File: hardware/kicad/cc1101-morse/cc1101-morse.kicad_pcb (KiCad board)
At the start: 2 copper layers, 40 x 60 mm, 15 parts, among them J1 Conn_02x04_Odd_Even, J2 Conn_01x04_Socket, SW1 SW_Push, U1 ESP32-C3-SuperMini

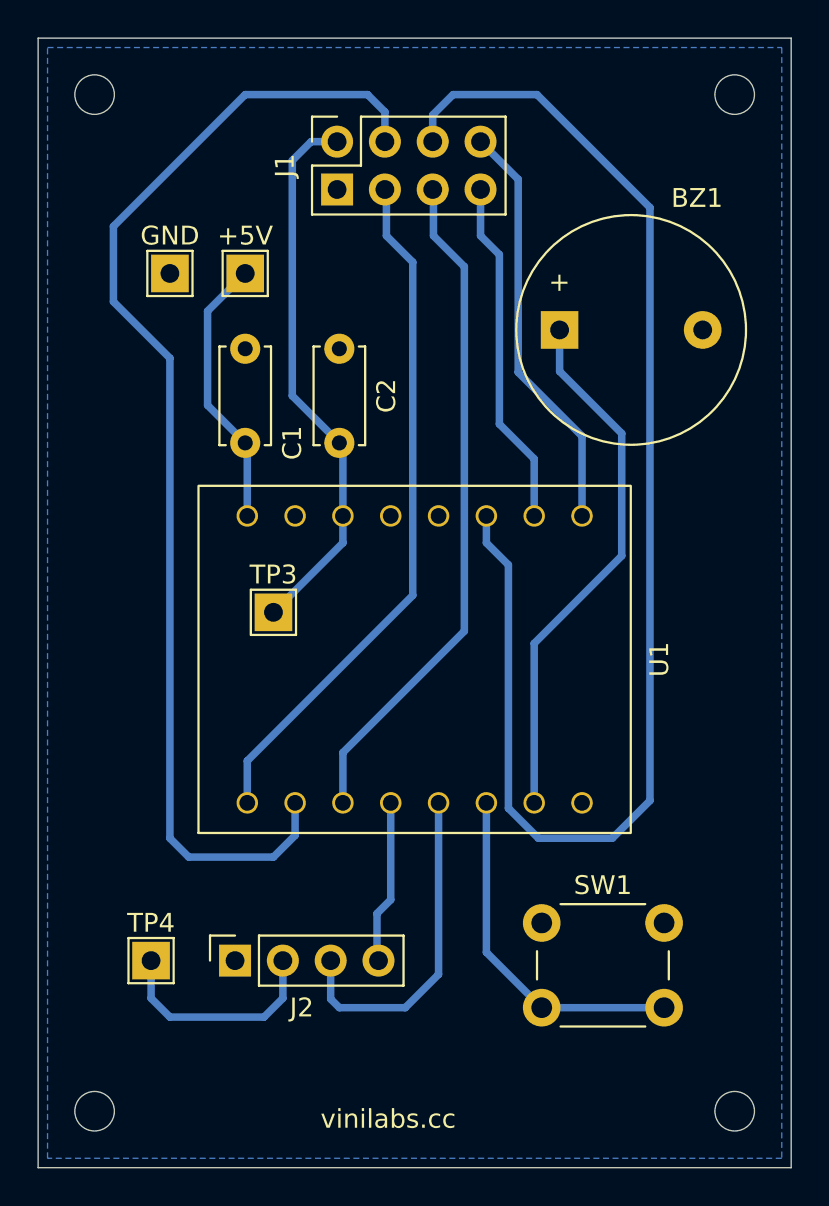
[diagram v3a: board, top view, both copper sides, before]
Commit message: Fixing routes
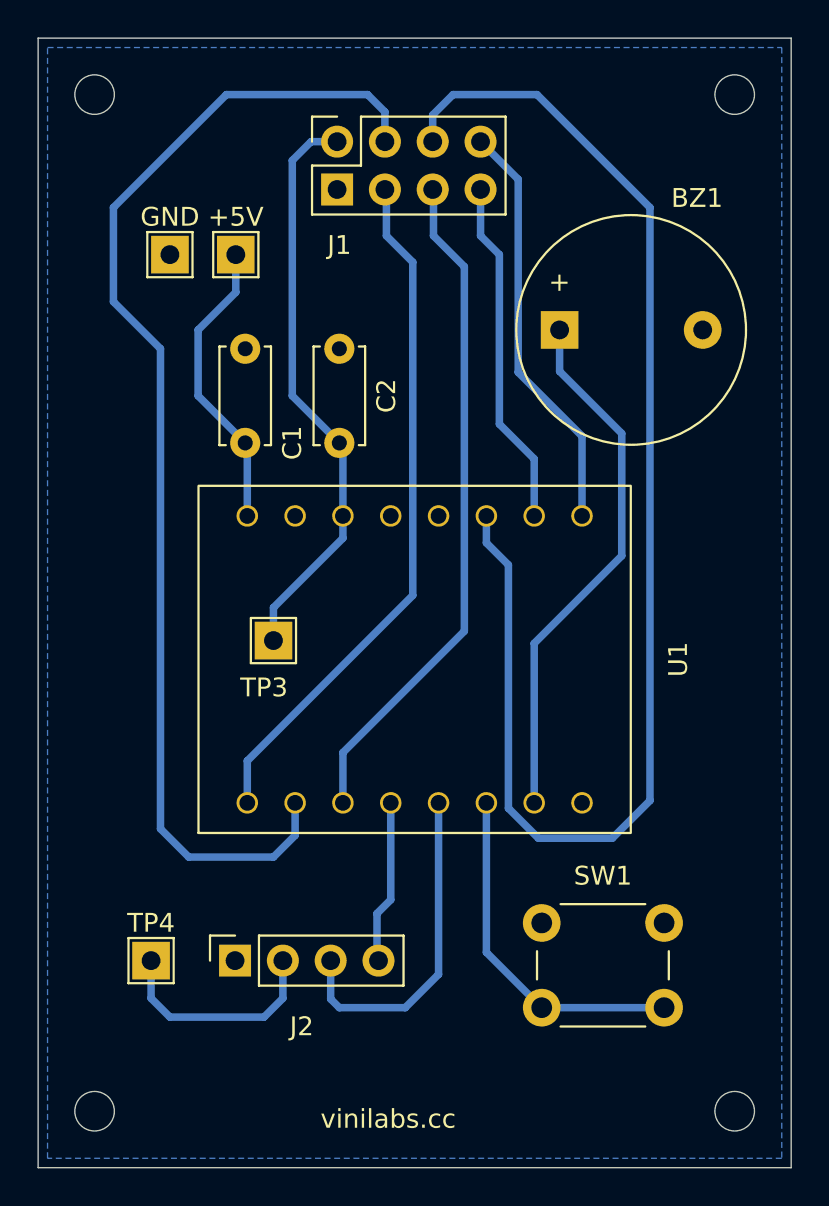
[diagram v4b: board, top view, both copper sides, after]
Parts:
- moved TP3 1.50 mm to (142.5, 102.5)
- moved TP1 1.12 mm to (140.5, 82.0)
- moved TP2 1.00 mm to (137.0, 82.0)
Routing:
- net +3V3: track 41.3 -> 42.8 mm
- net +5V: track 14.4 -> 15.6 mm
- net Net-(J1-Pin_4): track 62.3 -> 62.9 mm
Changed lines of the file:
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@@
 	(footprint "TestPoint:TestPoint_THTPad_2.0x2.0mm_Drill1.0mm"
 		(layer "F.Cu")
-		(at 142.5 101)
+		(at 142.5 102.5)
 		(descr "THT rectangular pad as test Point, square 2.0mm_Drill1.0mm  side length, hole diameter 1.0mm")
 		(tags "test point THT pad rectangle square")
 		(property "Reference" "TP3"
-			(at 0 -1.998 0)
+			(at -0.5 2.5 0)
 			(layer "F.SilkS")
 			(effects
@@
 			(layer "F.CrtYd")
 		)
-		(fp_text user "${REFERENCE}"
-			(at 0 -2 0)
-			(layer "F.Fab")
-			(effects
-				(font
-					(size 1 1)
-					(thickness 0.15)
-				)
-			)
-		)
 		(pad "1" thru_hole rect
 			(at 0 0)
@@
 	(footprint "TestPoint:TestPoint_THTPad_2.0x2.0mm_Drill1.0mm"
 		(layer "F.Cu")
-		(at 141 83)
+		(at 140.5 82)
 		(descr "THT rectangular pad as test Point, square 2.0mm_Drill1.0mm  side length, hole diameter 1.0mm")
 		(tags "test point THT pad rectangle square")
@@
 		(tags "tact sw push 6mm")
 		(property "Reference" "SW1"
-			(at 3.25 -2 0)
+			(at 3.25 -2.5 0)
 			(layer "F.SilkS")
 			(effects
@@
 	(footprint "TestPoint:TestPoint_THTPad_2.0x2.0mm_Drill1.0mm"
 		(layer "F.Cu")
-		(at 137 83)
+		(at 137 82)
 		(descr "THT rectangular pad as test Point, square 2.0mm_Drill1.0mm  side length, hole diameter 1.0mm")
 		(tags "test point THT pad rectangle square")
@@
 		(tags "Through hole socket strip THT 1x04 2.54mm single row")
 		(property "Reference" "J2"
-			(at -2.5 3.54 180)
+			(at -3.5 3.54 180)
 			(layer "F.SilkS")
 			(effects
@@
 		(at 150 103.5 90)
 		(property "Reference" "U1"
-			(at 0 13 90)
+			(at 0 14 90)
 			(unlocked yes)
 			(layer "F.SilkS")
@@
 		(tags "Through hole socket strip THT 2x04 2.54mm double row")
 		(property "Reference" "J1"
-			(at -1.27 -2.77 90)
+			(at -5.5 0.12 180)
 			(layer "F.SilkS")
 			(effects
@@
 	)
 	(segment
-		(start 146.19 97.31)
-		(end 146.19 95.88)
+		(start 146.19 97.06)
+		(end 142.5 100.75)
+		(width 0.4)
+		(layer "B.Cu")
+		(net "+3V3")
+	)
+	(segment
+		(start 142.5 100.75)
+		(end 142.5 102.5)
 		(width 0.4)
 		(layer "B.Cu")
@@
 	)
 	(segment
-		(start 142.5 101)
-		(end 146.19 97.31)
-		(width 0.4)
-		(layer "B.Cu")
-		(net "+3V3")
-	)
-	(segment
 		(start 146.19 95.88)
 		(end 146.19 92.19)
@@
 	)
 	(segment
-		(start 139 90)
-		(end 139 85)
+		(start 146.19 95.88)
+		(end 146.19 97.06)
+		(width 0.4)
+		(layer "B.Cu")
+		(net "+3V3")
+	)
+	(segment
+		(start 138.5 86)
+		(end 140.5 84)
 		(width 0.4)
 		(layer "B.Cu")
@@
 	)
 	(segment
-		(start 141 92)
-		(end 139 90)
+		(start 138.5 89.5)
+		(end 138.5 86)
 		(width 0.4)
 		(layer "B.Cu")
@@
 	)
 	(segment
-		(start 139 85)
-		(end 141 83)
+		(start 140.5 84)
+		(end 140.5 82)
 		(width 0.4)
 		(layer "B.Cu")
@@
 	)
 	(segment
+		(start 141 92)
+		(end 138.5 89.5)
+		(width 0.4)
+		(layer "B.Cu")
+		(net "+5V")
+	)
+	(segment
 		(start 153.81 111.12)
 		(end 153.81 119.06)
@@
 	)
 	(segment
+		(start 143.65 112.85)
+		(end 143.65 111.12)
+		(width 0.4)
+		(layer "B.Cu")
+		(net "Net-(J1-Pin_4)")
+	)
+	(segment
+		(start 138 114)
+		(end 142.5 114)
+		(width 0.4)
+		(layer "B.Cu")
+		(net "Net-(J1-Pin_4)")
+	)
+	(segment
 		(start 148.42 74.42)
 		(end 147.5 73.5)
@@
 	)
 	(segment
+		(start 136.5 87)
+		(end 136.5 112.5)
+		(width 0.4)
+		(layer "B.Cu")
+		(net "Net-(J1-Pin_4)")
+	)
+	(segment
+		(start 148.42 76)
+		(end 148.42 74.42)
+		(width 0.4)
+		(layer "B.Cu")
+		(net "Net-(J1-Pin_4)")
+	)
+	(segment
+		(start 147.5 73.5)
+		(end 140 73.5)
+		(width 0.4)
+		(layer "B.Cu")
+		(net "Net-(J1-Pin_4)")
+	)
+	(segment
+		(start 140 73.5)
+		(end 134 79.5)
+		(width 0.4)
+		(layer "B.Cu")
+		(net "Net-(J1-Pin_4)")
+	)
+	(segment
 		(start 142.5 114)
 		(end 143.65 112.85)
@@
 	)
 	(segment
-		(start 137 87.5)
-		(end 137 113)
+		(start 134 84.5)
+		(end 136.5 87)
 		(width 0.4)
 		(layer "B.Cu")
@@
 	)
 	(segment
-		(start 138 114)
-		(end 142.5 114)
+		(start 136.5 112.5)
+		(end 138 114)
 		(width 0.4)
 		(layer "B.Cu")
@@
 	)
 	(segment
-		(start 137 113)
-		(end 138 114)
-		(width 0.4)
-		(layer "B.Cu")
-		(net "Net-(J1-Pin_4)")
-	)
-	(segment
-		(start 147.5 73.5)
-		(end 141 73.5)
-		(width 0.4)
-		(layer "B.Cu")
-		(net "Net-(J1-Pin_4)")
-	)
-	(segment
-		(start 134 80.5)
+		(start 134 79.5)
 		(end 134 84.5)
 		(width 0.4)
 		(layer "B.Cu")
-		(net "Net-(J1-Pin_4)")
-	)
-	(segment
-		(start 148.42 76)
-		(end 148.42 74.42)
-		(width 0.4)
-		(layer "B.Cu")
-		(net "Net-(J1-Pin_4)")
-	)
-	(segment
-		(start 141 73.5)
-		(end 134 80.5)
-		(width 0.4)
-		(layer "B.Cu")
-		(net "Net-(J1-Pin_4)")
-	)
-	(segment
-		(start 143.65 112.85)
-		(end 143.65 111.12)
-		(width 0.4)
-		(layer "B.Cu")
-		(net "Net-(J1-Pin_4)")
-	)
-	(segment
-		(start 134 84.5)
-		(end 137 87.5)
-		(width 0.4)
-		(layer "B.Cu")
